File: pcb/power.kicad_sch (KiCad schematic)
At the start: 20 parts, among them J17 12-24v DC, J18 5V Supply, Q1 DMP3028LK3-13, U4 AP2114-3.3, U5 AP63205WU

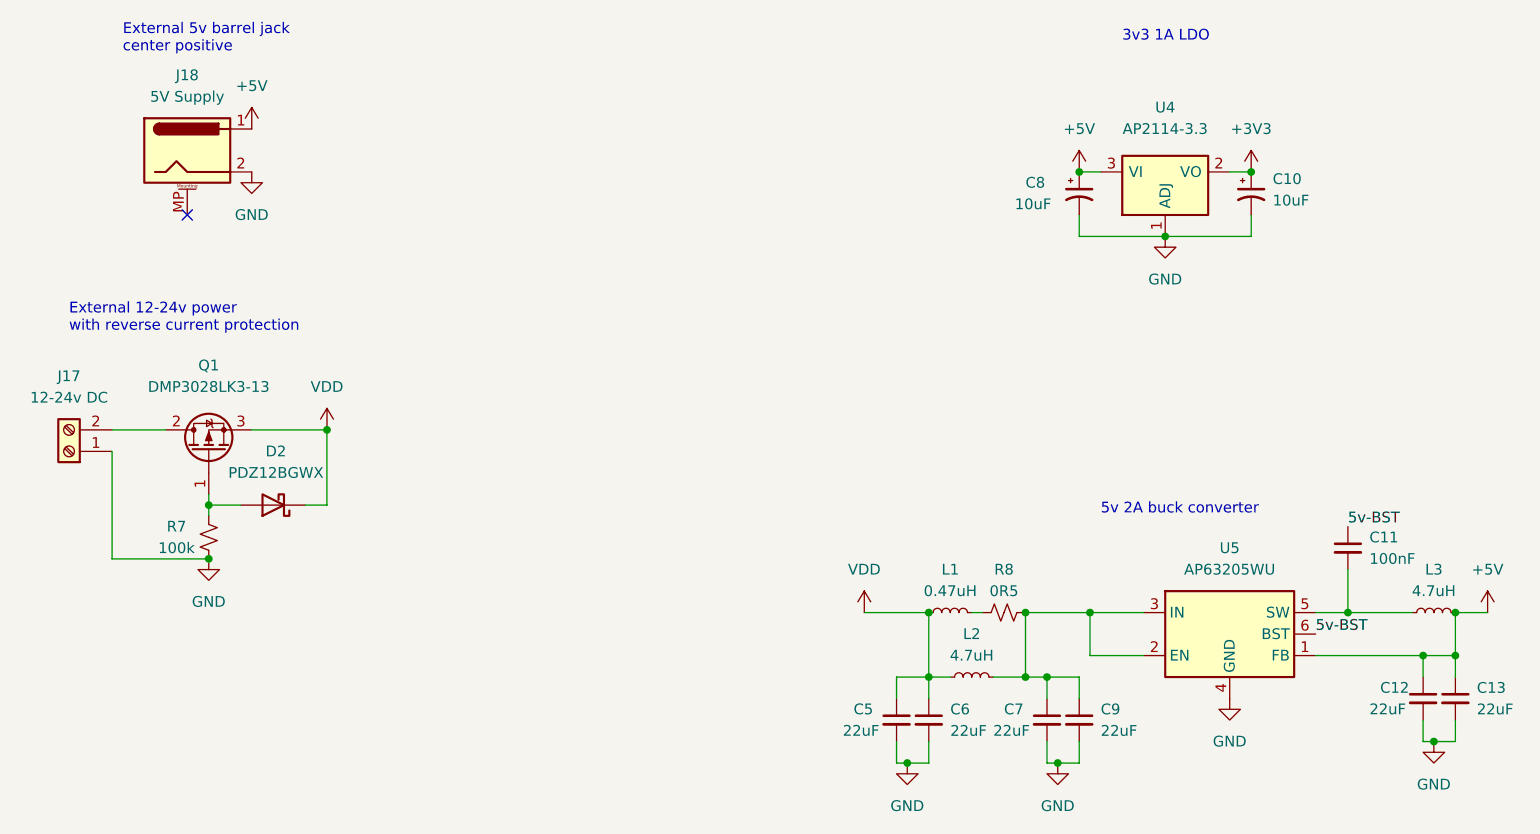
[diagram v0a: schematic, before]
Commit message: Exclude R3 and R9 from population.
Upgrades files to KiCad 7.x.

Fixes: https://github.com/atanisoft/Esp32FeederController/issues/10
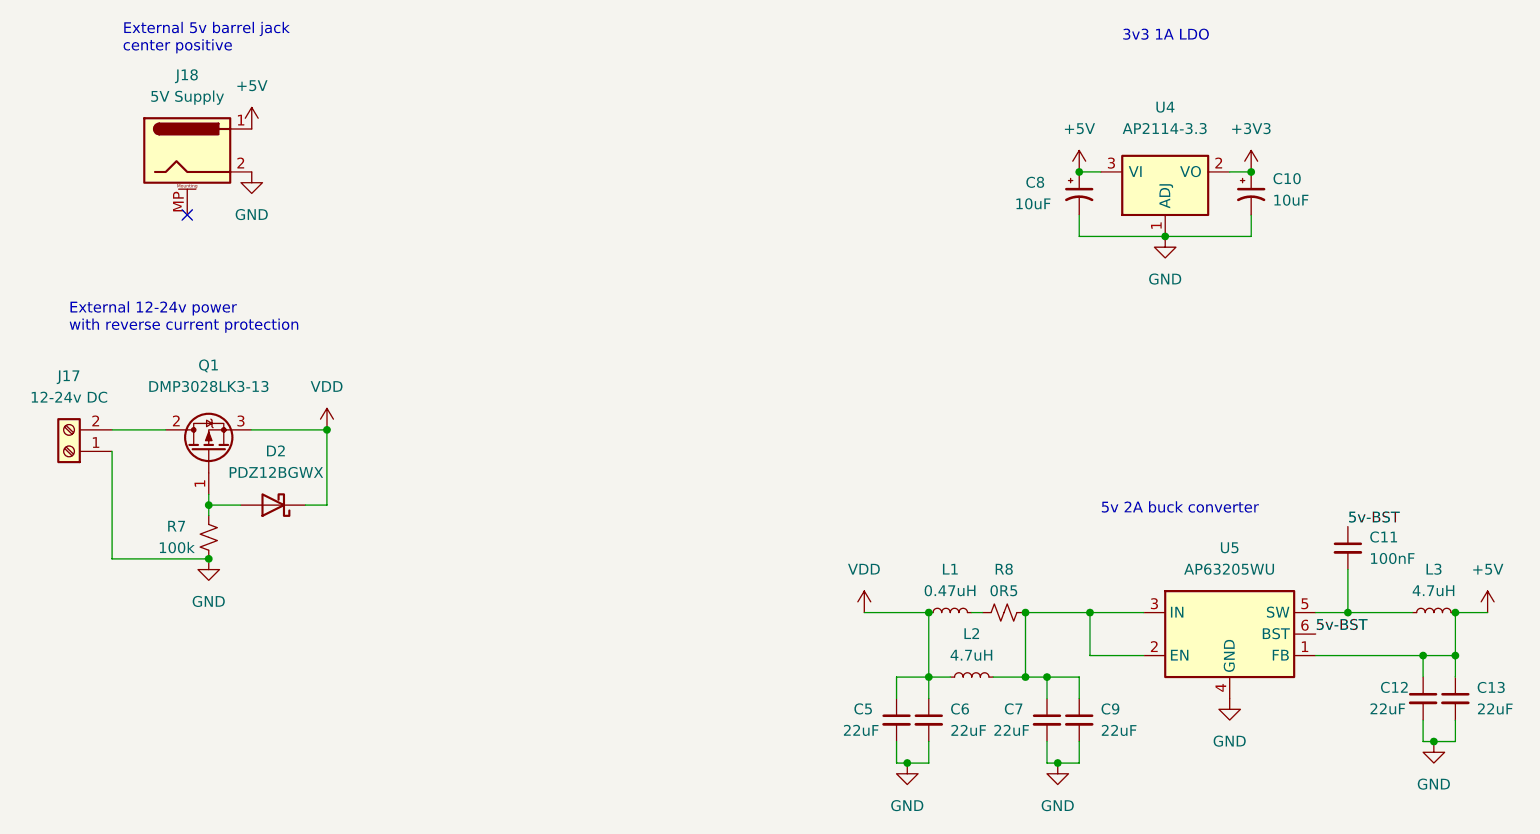
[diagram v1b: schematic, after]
